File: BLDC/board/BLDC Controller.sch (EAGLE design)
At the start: 113 parts, among them IC1 DRV8301, IC2 OPA2374, IC3 Encoder, IC4 INA199A1, IC5 TPS51103, M1 FRDM-KL05Z, M2 MBED_NXP_LPC1768, Q1 MOSFET-NCHANNELSMD, Q2 MOSFET-NCHANNELSMD, Q3 P-CHANNEL-MOSFETTO252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

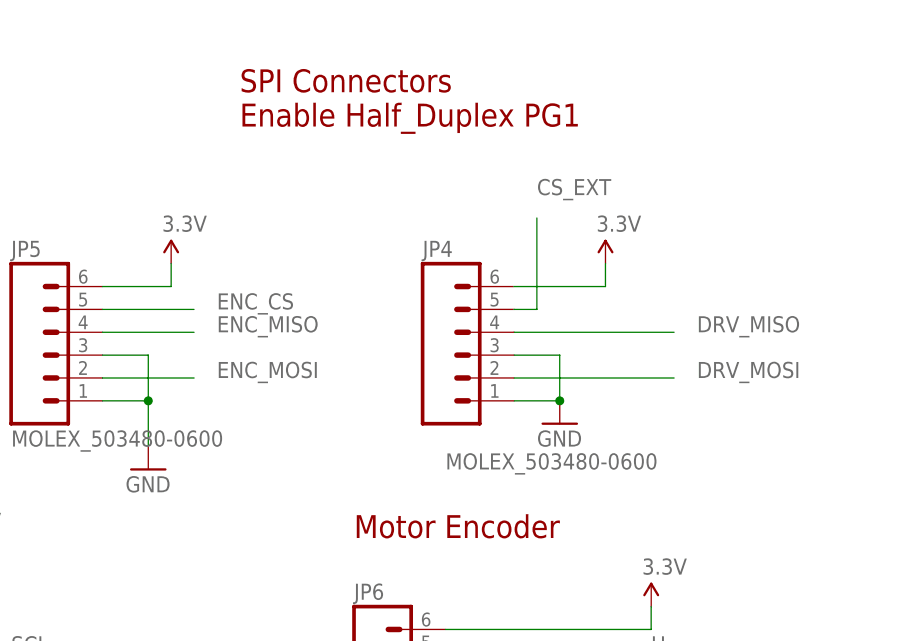
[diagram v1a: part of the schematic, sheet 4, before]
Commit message: Fixed DRC to have 6mil clearance, fixed DRC errors.
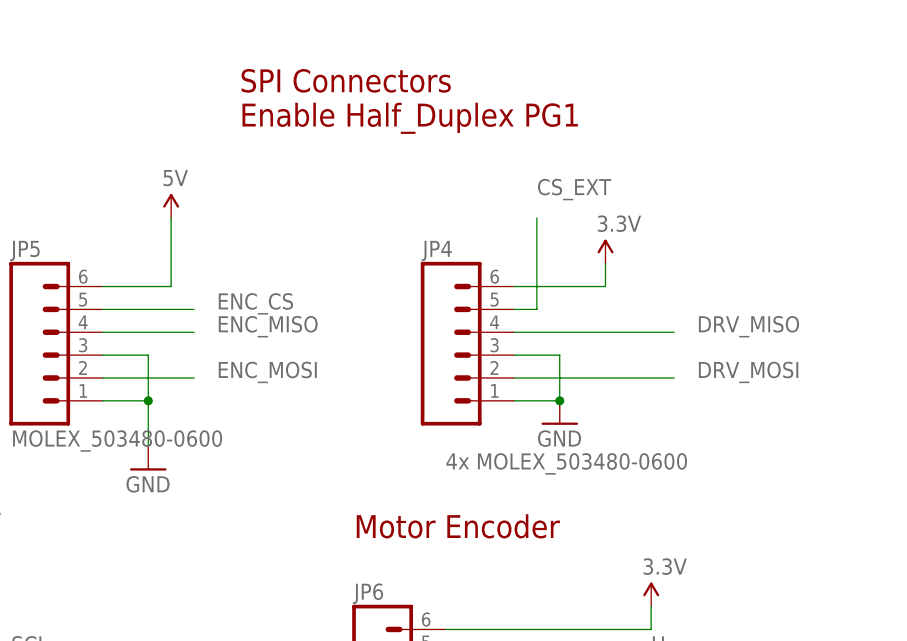
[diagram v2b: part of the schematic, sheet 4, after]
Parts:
- removed IC4: INA199A1, modular_robotics:INA199A1
- IC3: value Encoder -> AS 5134
- JP4: value MOLEX_503480-0600 -> 4x MOLEX_503480-0600
- renumbered U$4 to ICN, U$8 to S2
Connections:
- net 3.3V: no longer JP5.6
- net 5V: now also JP5.6
- net GND: now also ICNG$2.REF; no longer IC4G$2.REF
- net I_BATT: now also ICNG$2.+IN; no longer IC4G$2.+IN
- net N$18: now also ICNG$2.OUT; no longer IC4G$2.OUT
- net V_BATT: now also ICNG$2.-IN; no longer IC4G$2.-IN
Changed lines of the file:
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@@
 <part name="P+4" library="biomimetic" deviceset="3.3V" device=""/>
 <part name="GND30" library="biomimetic" deviceset="GND" device=""/>
-<part name="JP4" library="biomimetic" deviceset="MOLEX_503480-0600" device=""/>
+<part name="JP4" library="biomimetic" deviceset="MOLEX_503480-0600" device="" value="4x MOLEX_503480-0600"/>
 <part name="P+10" library="biomimetic" deviceset="3.3V" device=""/>
 <part name="GND31" library="biomimetic" deviceset="GND" device=""/>
@@
 <part name="GND32" library="biomimetic" deviceset="GND" device=""/>
 <part name="FRAME5" library="biomimetic" deviceset="FRAME-LETTER" device=""/>
-<part name="IC3" library="biomimetic" deviceset="AS5134" device="" value="Encoder"/>
+<part name="IC3" library="biomimetic" deviceset="AS5134" device="" value="AS 5134"/>
 <part name="C28" library="biomimetic" deviceset="CAP" device="0402-CAP" value="100nF"/>
 <part name="GND33" library="biomimetic" deviceset="GND" device=""/>
@@
 <part name="GND45" library="biomimetic" deviceset="GND" device=""/>
 <part name="GND46" library="biomimetic" deviceset="GND" device=""/>
-<part name="IC4" library="modular_robotics" deviceset="INA199A1" device=""/>
 <part name="U$17" library="modular_robotics" deviceset="V_BATT" device=""/>
 <part name="R38" library="biomimetic" deviceset="RESISTOR" device="0402-RES" value="1k"/>
@@
 <part name="C29" library="biomimetic" deviceset="CAP" device="0402-CAP" value="100nF"/>
 <part name="R30" library="biomimetic" deviceset="RESISTOR" device="2010" value=".01"/>
-<part name="U$4" library="modular_robotics" deviceset="INA199A1" device=""/>
 <part name="GND35" library="biomimetic" deviceset="GND" device=""/>
 <part name="U$5" library="biomimetic" deviceset="V_BATT" device=""/>
@@
 <part name="JP8" library="pinhead" deviceset="PINHD-1X4" device="" value="UVW_Out"/>
 <part name="GND39" library="biomimetic" deviceset="GND" device=""/>
-<part name="P+12" library="biomimetic" deviceset="3.3V" device=""/>
 <part name="GND40" library="biomimetic" deviceset="GND" device=""/>
 <part name="SJ2" library="jumper" deviceset="SJ" device=""/>
 <part name="SJ6" library="jumper" deviceset="SJ" device=""/>
 <part name="GND47" library="biomimetic" deviceset="GND" device=""/>
-<part name="U$8" library="modular_robotics" deviceset="JS202011SCQN" device=""/>
+<part name="S2" library="modular_robotics" deviceset="JS202011SCQN" device=""/>
 <part name="GND49" library="biomimetic" deviceset="GND" device=""/>
 <part name="GND50" library="biomimetic" deviceset="GND" device=""/>
@@
 <part name="LED5" library="biomimetic" deviceset="LED" device="0603" value="GREEN"/>
 <part name="R25" library="biomimetic" deviceset="RESISTOR" device="0603-RES" value="4.99k"/>
+<part name="ICN" library="modular_robotics" deviceset="INA199A1" device=""/>
+<part name="U$4" library="biomimetic" deviceset="5V" device=""/>
 </parts>
 <sheets>
@@
 <instance part="SJ5" gate="1" x="187.96" y="96.52" rot="R90"/>
 <instance part="GND47" gate="1" x="40.64" y="17.78" rot="R270"/>
-<instance part="U$8" gate="G$1" x="48.26" y="111.76" rot="R90"/>
-<instance part="U$8" gate="G$2" x="48.26" y="121.92" rot="R90"/>
+<instance part="S2" gate="G$1" x="48.26" y="111.76" rot="R90"/>
+<instance part="S2" gate="G$2" x="48.26" y="121.92" rot="R90"/>
 <instance part="GND49" gate="1" x="17.78" y="111.76" rot="R270"/>
 <instance part="GND50" gate="1" x="7.62" y="124.46" rot="R270"/>
@@
 <segment>
 <pinref part="GND49" gate="1" pin="GND"/>
-<pinref part="U$8" gate="G$1" pin="O"/>
+<pinref part="S2" gate="G$1" pin="O"/>
 <wire x1="20.32" y1="111.76" x2="43.18" y2="111.76" width="0.1524" layer="91"/>
 </segment>
@@
 <segment>
 <pinref part="P+14" gate="G$1" pin="3.3V"/>
-<pinref part="U$8" gate="G$2" pin="P"/>
+<pinref part="S2" gate="G$2" pin="P"/>
 <wire x1="55.88" y1="121.92" x2="53.34" y2="121.92" width="0.1524" layer="91"/>
 </segment>
@@
 <net name="ENABLE" class="0">
 <segment>
-<pinref part="U$8" gate="G$1" pin="S"/>
+<pinref part="S2" gate="G$1" pin="S"/>
 <wire x1="43.18" y1="116.84" x2="17.78" y2="116.84" width="0.1524" layer="91"/>
 <label x="17.78" y="116.84" size="1.778" layer="95"/>
@@
 <pinref part="LED5" gate="G$1" pin="A"/>
 <wire x1="35.56" y1="124.46" x2="43.18" y2="124.46" width="0.1524" layer="91"/>
-<pinref part="U$8" gate="G$2" pin="S"/>
+<pinref part="S2" gate="G$2" pin="S"/>
 </segment>
 </net>
@@
 <pinref part="IC1" gate="G$1" pin="EN_GATE"/>
 <label x="91.44" y="124.46" size="1.27" layer="95"/>
-<pinref part="U$8" gate="G$1" pin="P"/>
+<pinref part="S2" gate="G$1" pin="P"/>
 <wire x1="53.34" y1="114.3" x2="63.5" y2="114.3" width="0.1524" layer="91"/>
 <wire x1="63.5" y1="114.3" x2="63.5" y2="124.46" width="0.1524" layer="91"/>
@@
 <instance part="C29" gate="G$1" x="195.58" y="114.3"/>
 <instance part="R30" gate="G$1" x="167.64" y="139.7" rot="R180"/>
-<instance part="IC4" gate="G$2" x="137.16" y="68.58"/>
-<instance part="U$4" gate="G$1" x="134.62" y="68.58"/>
 <instance part="GND35" gate="1" x="134.62" y="53.34"/>
 <instance part="U$5" gate="G$1" x="134.62" y="81.28"/>
 <instance part="GND36" gate="1" x="144.78" y="78.74" rot="R90"/>
+<instance part="ICN" gate="G$1" x="134.62" y="68.58"/>
+<instance part="ICN" gate="G$2" x="137.16" y="68.58"/>
 </instances>
 <busses>
@@
 <segment>
 <pinref part="GND35" gate="1" pin="GND"/>
-<pinref part="U$4" gate="G$1" pin="GND"/>
 <wire x1="134.62" y1="55.88" x2="134.62" y2="58.42" width="0.1524" layer="91"/>
-</segment>
-<segment>
-<pinref part="IC4" gate="G$2" pin="REF"/>
+<pinref part="ICN" gate="G$1" pin="GND"/>
+</segment>
+<segment>
 <wire x1="137.16" y1="76.2" x2="137.16" y2="78.74" width="0.1524" layer="91"/>
 <pinref part="GND36" gate="1" pin="GND"/>
 <wire x1="137.16" y1="78.74" x2="142.24" y2="78.74" width="0.1524" layer="91"/>
+<pinref part="ICN" gate="G$2" pin="REF"/>
 </segment>
 </net>
@@
 <wire x1="129.54" y1="66.04" x2="121.92" y2="66.04" width="0.1524" layer="91"/>
 <pinref part="U$17" gate="G$1" pin="V_BATT"/>
-<pinref part="IC4" gate="G$2" pin="-IN"/>
-</segment>
-<segment>
-<pinref part="U$4" gate="G$1" pin="V+"/>
+<pinref part="ICN" gate="G$2" pin="-IN"/>
+</segment>
+<segment>
 <pinref part="U$5" gate="G$1" pin="V_BATT"/>
 <wire x1="134.62" y1="78.74" x2="134.62" y2="81.28" width="0.1524" layer="91"/>
+<pinref part="ICN" gate="G$1" pin="V+"/>
 </segment>
 </net>
@@
 <wire x1="129.54" y1="71.12" x2="121.92" y2="71.12" width="0.1524" layer="91"/>
 <label x="121.92" y="71.12" size="1.778" layer="95"/>
-<pinref part="IC4" gate="G$2" pin="+IN"/>
+<pinref part="ICN" gate="G$2" pin="+IN"/>
 </segment>
 <segment>
@@
 <segment>
 <pinref part="R38" gate="G$1" pin="2"/>
-<pinref part="IC4" gate="G$2" pin="OUT"/>
+<pinref part="ICN" gate="G$2" pin="OUT"/>
 </segment>
 </net>
@@
 <instance part="JP8" gate="A" x="231.14" y="144.78"/>
 <instance part="GND39" gate="1" x="203.2" y="152.4" rot="R180"/>
-<instance part="P+12" gate="G$1" x="162.56" y="101.6"/>
 <instance part="GND40" gate="1" x="160.02" y="78.74"/>
+<instance part="U$4" gate="G$1" x="162.56" y="106.68"/>
 </instances>
 <busses>
@@
 <pinref part="P+11" gate="G$1" pin="3.3V"/>
 <wire x1="215.9" y1="60.96" x2="215.9" y2="63.5" width="0.1524" layer="91"/>
-</segment>
-<segment>
-<pinref part="JP5" gate="G$1" pin="6"/>
-<pinref part="P+12" gate="G$1" pin="3.3V"/>
-<wire x1="154.94" y1="99.06" x2="162.56" y2="99.06" width="0.1524" layer="91"/>
-<wire x1="162.56" y1="99.06" x2="162.56" y2="101.6" width="0.1524" layer="91"/>
 </segment>
 </net>
@@
 </segment>
 </net>
+<net name="5V" class="0">
+<segment>
+<pinref part="JP5" gate="G$1" pin="6"/>
+<wire x1="154.94" y1="99.06" x2="162.56" y2="99.06" width="0.1524" layer="91"/>
+<pinref part="U$4" gate="G$1" pin="5V"/>
+<wire x1="162.56" y1="99.06" x2="162.56" y2="106.68" width="0.1524" layer="91"/>
+</segment>
+</net>
